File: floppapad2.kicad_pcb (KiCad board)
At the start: 2 copper layers, 76.2 x 76.2 mm, 43 parts, among them J1 USBC, J2 DBG, SW1 SW_Push, SW10 SW_Push, SW11 RotaryEncoder_Switch, SW12 BOOT, SW2 SW_Push, SW3 SW_Push, SW4 SW_Push, SW5 SW_Push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

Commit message: slight adjustment
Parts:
- moved C13 7.47 mm to (63.8, 104.7), turned to -90 degrees
- moved C11 0.91 mm to (59.7, 110.4)
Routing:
- net +3.3V: track 69.0 -> 66.4 mm

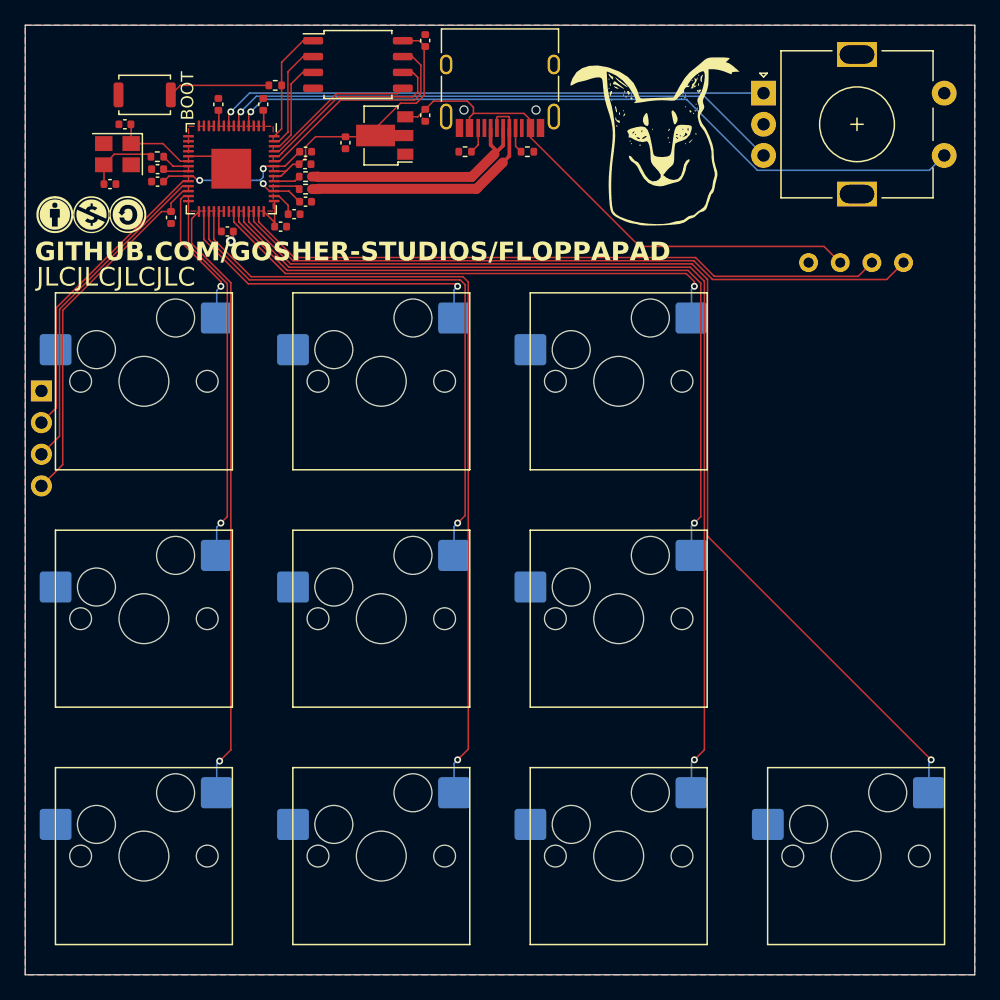
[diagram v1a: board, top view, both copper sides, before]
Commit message: mounting holes
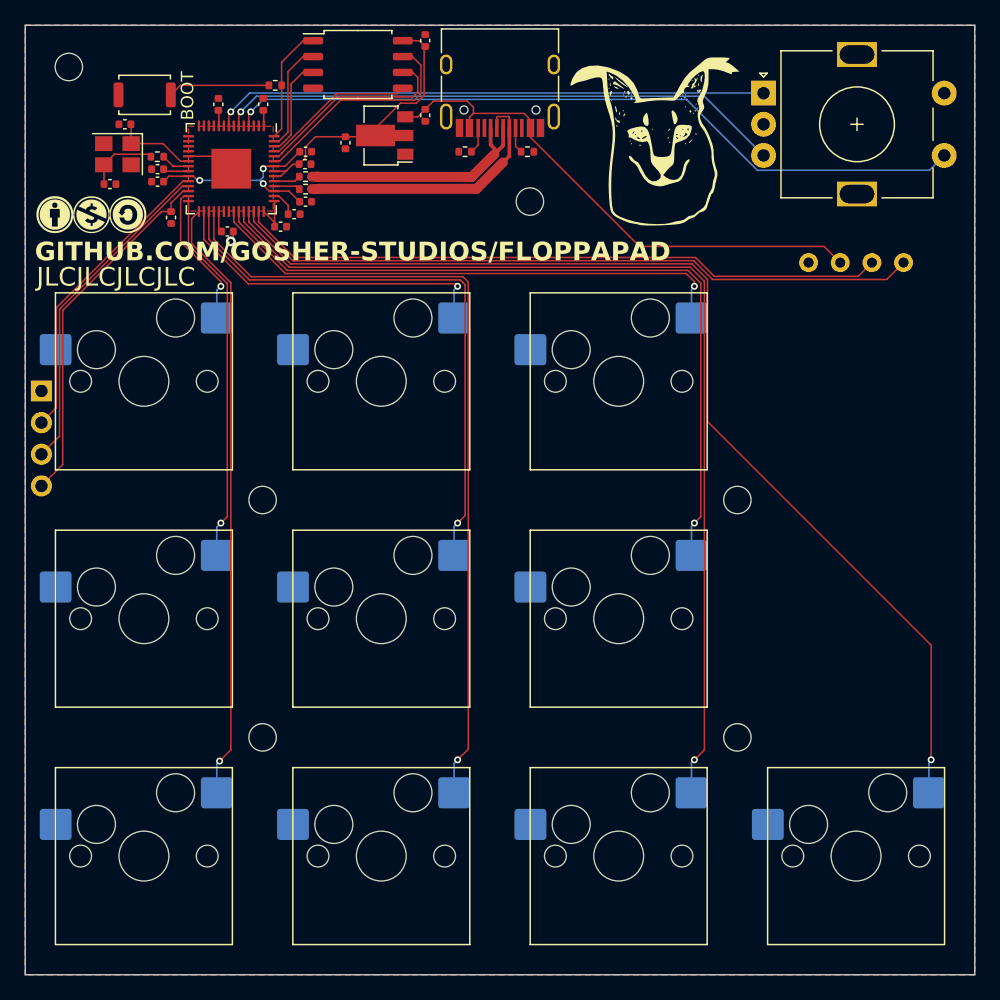
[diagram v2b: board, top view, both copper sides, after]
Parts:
- added REF**: M2, MountingHole:MountingHole_2.2mm_M2, F.Cu at (57.1, 133.3)
- added REF**: M2, MountingHole:MountingHole_2.2mm_M2, F.Cu at (95.2, 133.3)
- added REF**: M2, MountingHole:MountingHole_2.2mm_M2, F.Cu at (78.6, 109.4)
- added REF**: M2, MountingHole:MountingHole_2.2mm_M2, F.Cu at (41.6, 98.6)
- added REF**: M2, MountingHole:MountingHole_2.2mm_M2, F.Cu at (95.2, 152.4)
- added REF**: M2, MountingHole:MountingHole_2.2mm_M2, F.Cu at (57.1, 152.4)
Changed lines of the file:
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@@
     )
   )
+  (footprint "MountingHole:MountingHole_2.2mm_M2" (layer "F.Cu")
+    (at 57.15 133.35)
+    (descr "Mounting Hole 2.2mm, no annular, M2")
+    (tags "mounting hole 2.2mm no annular m2")
+    (attr exclude_from_pos_files exclude_from_bom)
+    (fp_text reference "REF**" (at 0 -3.2) (layer "F.SilkS") hide
+        (effects (font (size 1 1) (thickness 0.15)))
+    )
+    (fp_text value "M2" (at 0 3.2) (layer "F.Fab")
+        (effects (font (size 1 1) (thickness 0.15)))
+    )
+    (fp_text user "${REFERENCE}" (at 0 0) (layer "F.Fab")
+        (effects (font (size 1 1) (thickness 0.15)))
+    )
+    (fp_circle (center 0 0) (end 2.2 0)
+      (stroke (width 0.15) (type solid)) (fill none) (layer "Cmts.User"))
+    (fp_circle (center 0 0) (end 2.45 0)
+      (stroke (width 0.05) (type solid)) (fill none) (layer "F.CrtYd"))
+    (pad "" np_thru_hole circle (at 0 0) (size 2.2 2.2) (drill 2.2) (layers "F&B.Cu" "*.Mask"))
+  )
   (footprint "Package_SO:SOIC-8_5.23x5.23mm_P1.27mm" (layer "F.Cu")
     (at 64.8 98.4)
@@
     )
   )
+  (footprint "MountingHole:MountingHole_2.2mm_M2" (layer "F.Cu")
+    (at 95.25 133.35)
+    (descr "Mounting Hole 2.2mm, no annular, M2")
+    (tags "mounting hole 2.2mm no annular m2")
+    (attr exclude_from_pos_files exclude_from_bom)
+    (fp_text reference "REF**" (at 0 -3.2) (layer "F.SilkS") hide
+        (effects (font (size 1 1) (thickness 0.15)))
+    )
+    (fp_text value "M2" (at 0 3.2) (layer "F.Fab")
+        (effects (font (size 1 1) (thickness 0.15)))
+    )
+    (fp_text user "${REFERENCE}" (at 0 0) (layer "F.Fab")
+        (effects (font (size 1 1) (thickness 0.15)))
+    )
+    (fp_circle (center 0 0) (end 2.2 0)
+      (stroke (width 0.15) (type solid)) (fill none) (layer "Cmts.User"))
+    (fp_circle (center 0 0) (end 2.45 0)
+      (stroke (width 0.05) (type solid)) (fill none) (layer "F.CrtYd"))
+    (pad "" np_thru_hole circle (at 0 0) (size 2.2 2.2) (drill 2.2) (layers "F&B.Cu" "*.Mask"))
+  )
   (footprint "kiswitch:SW_Hotswap_Kailh_MX_1.00u" (layer "F.Cu")
     (at 66.675 123.825)
@@
     )
   )
+  (footprint "MountingHole:MountingHole_2.2mm_M2" (layer "F.Cu")
+    (at 78.6 109.4)
+    (descr "Mounting Hole 2.2mm, no annular, M2")
+    (tags "mounting hole 2.2mm no annular m2")
+    (attr exclude_from_pos_files exclude_from_bom)
+    (fp_text reference "REF**" (at 0 -3.2) (layer "F.SilkS") hide
+        (effects (font (size 1 1) (thickness 0.15)))
+    )
+    (fp_text value "M2" (at 0 3.2) (layer "F.Fab")
+        (effects (font (size 1 1) (thickness 0.15)))
+    )
+    (fp_text user "${REFERENCE}" (at 0 0) (layer "F.Fab")
+        (effects (font (size 1 1) (thickness 0.15)))
+    )
+    (fp_circle (center 0 0) (end 2.2 0)
+      (stroke (width 0.15) (type solid)) (fill none) (layer "Cmts.User"))
+    (fp_circle (center 0 0) (end 2.45 0)
+      (stroke (width 0.05) (type solid)) (fill none) (layer "F.CrtYd"))
+    (pad "" np_thru_hole circle (at 0 0) (size 2.2 2.2) (drill 2.2) (layers "F&B.Cu" "*.Mask"))
+  )
   (footprint "Capacitor_SMD:C_0402_1005Metric" (layer "F.Cu")
     (at 60.595 109.4125)
@@
     )
   )
+  (footprint "MountingHole:MountingHole_2.2mm_M2" (layer "F.Cu")
+    (at 41.6 98.6)
+    (descr "Mounting Hole 2.2mm, no annular, M2")
+    (tags "mounting hole 2.2mm no annular m2")
+    (attr exclude_from_pos_files exclude_from_bom)
+    (fp_text reference "REF**" (at 0 -3.2) (layer "F.SilkS") hide
+        (effects (font (size 1 1) (thickness 0.15)))
+    )
+    (fp_text value "M2" (at 0 3.2) (layer "F.Fab")
+        (effects (font (size 1 1) (thickness 0.15)))
+    )
+    (fp_text user "${REFERENCE}" (at 0 0) (layer "F.Fab")
+        (effects (font (size 1 1) (thickness 0.15)))
+    )
+    (fp_circle (center 0 0) (end 2.2 0)
+      (stroke (width 0.15) (type solid)) (fill none) (layer "Cmts.User"))
+    (fp_circle (center 0 0) (end 2.45 0)
+      (stroke (width 0.05) (type solid)) (fill none) (layer "F.CrtYd"))
+    (pad "" np_thru_hole circle (at 0 0) (size 2.2 2.2) (drill 2.2) (layers "F&B.Cu" "*.Mask"))
+  )
   (footprint "kiswitch:SW_Hotswap_Kailh_MX_1.00u" (layer "F.Cu")
     (at 66.675 142.875)
@@
     )
   )
+  (footprint "MountingHole:MountingHole_2.2mm_M2" (layer "F.Cu")
+    (at 95.25 152.4)
+    (descr "Mounting Hole 2.2mm, no annular, M2")
+    (tags "mounting hole 2.2mm no annular m2")
+    (attr exclude_from_pos_files exclude_from_bom)
+    (fp_text reference "REF**" (at 0 -3.2) (layer "F.SilkS") hide
+        (effects (font (size 1 1) (thickness 0.15)))
+    )
+    (fp_text value "M2" (at 0 3.2) (layer "F.Fab")
+        (effects (font (size 1 1) (thickness 0.15)))
+    )
+    (fp_text user "${REFERENCE}" (at 0 0) (layer "F.Fab")
+        (effects (font (size 1 1) (thickness 0.15)))
+    )
+    (fp_circle (center 0 0) (end 2.2 0)
+      (stroke (width 0.15) (type solid)) (fill none) (layer "Cmts.User"))
+    (fp_circle (center 0 0) (end 2.45 0)
+      (stroke (width 0.05) (type solid)) (fill none) (layer "F.CrtYd"))
+    (pad "" np_thru_hole circle (at 0 0) (size 2.2 2.2) (drill 2.2) (layers "F&B.Cu" "*.Mask"))
+  )
   (footprint "kiswitch:SW_Hotswap_Kailh_MX_1.00u" (layer "F.Cu")
     (at 104.775 161.925)
@@
     )
   )
+  (footprint "MountingHole:MountingHole_2.2mm_M2" (layer "F.Cu")
+    (at 57.15 152.4)
+    (descr "Mounting Hole 2.2mm, no annular, M2")
+    (tags "mounting hole 2.2mm no annular m2")
+    (attr exclude_from_pos_files exclude_from_bom)
+    (fp_text reference "REF**" (at 0 -3.2) (layer "F.SilkS") hide
+        (effects (font (size 1 1) (thickness 0.15)))
+    )
+    (fp_text value "M2" (at 0 3.2) (layer "F.Fab")
+        (effects (font (size 1 1) (thickness 0.15)))
+    )
+    (fp_text user "${REFERENCE}" (at 0 0) (layer "F.Fab")
+        (effects (font (size 1 1) (thickness 0.15)))
+    )
+    (fp_circle (center 0 0) (end 2.2 0)
+      (stroke (width 0.15) (type solid)) (fill none) (layer "Cmts.User"))
+    (fp_circle (center 0 0) (end 2.45 0)
+      (stroke (width 0.05) (type solid)) (fill none) (layer "F.CrtYd"))
+    (pad "" np_thru_hole circle (at 0 0) (size 2.2 2.2) (drill 2.2) (layers "*.Cu" "*.Mask"))
+  )
   (footprint "floppapad2:floppa" (layer "F.Cu")
     (at 88.6 104.6)
@@
   (segment (start 72.517 135.483) (end 72.8 135.2) (width 0.127) (layer "B.Cu") (net 25))
   (segment (start 72.517 137.795) (end 72.517 135.483) (width 0.127) (layer "B.Cu") (net 25))
-  (segment (start 55.2375 110.2) (end 55.2375 111.0375) (width 0.127) (layer "F.Cu") (net 26))
-  (segment (start 92.3135 115.950401) (end 92.3135 134.6865) (width 0.127) (layer "F.Cu") (net 26))
-  (segment (start 92.3135 134.6865) (end 91.8 135.2) (width 0.127) (layer "F.Cu") (net 26))
   (segment (start 59.1245 114.9245) (end 91.287599 114.9245) (width 0.127) (layer "F.Cu") (net 26))
+  (segment (start 92.3135 134.6865) (end 91.8 135.2) (width 0.127) (layer "F.Cu") (net 26))
   (segment (start 55.2375 111.0375) (end 59.1245 114.9245) (width 0.127) (layer "F.Cu") (net 26))
+  (segment (start 55.2375 110.2) (end 55.2375 111.0375) (width 0.127) (layer "F.Cu") (net 26))
+  (segment (start 92.3135 115.950401) (end 92.3135 134.6865) (width 0.127) (layer "F.Cu") (net 26))
   (segment (start 91.287599 114.9245) (end 92.3135 115.950401) (width 0.127) (layer "F.Cu") (net 26))
   (via (at 91.8 135.2) (size 0.56) (drill 0.3) (layers "F.Cu" "B.Cu") (net 26))
@@
   (segment (start 91.8 154.2) (end 91.567 154.433) (width 0.127) (layer "B.Cu") (net 29))
   (segment (start 91.567 154.433) (end 91.567 156.845) (width 0.127) (layer "B.Cu") (net 29))
-  (segment (start 56.0375 110.2) (end 56.0375 111.0375) (width 0.127) (layer "F.Cu") (net 30))
   (segment (start 56.0375 111.0375) (end 59.4 114.4) (width 0.127) (layer "F.Cu") (net 30))
-  (segment (start 92.854 136.254) (end 110.8 154.2) (width 0.127) (layer "F.Cu") (net 30))
-  (segment (start 59.4 114.4) (end 91.6 114.4) (width 0.127) (layer "F.Cu") (net 30))
-  (segment (start 92.854 115.654) (end 92.854 136.254) (width 0.127) (layer "F.Cu") (net 30))
+  (segment (start 110.8 145) (end 110.8 154.2) (width 0.127) (layer "F.Cu") (net 30))
+  (segment (start 92.854 127.054) (end 110.8 145) (width 0.127) (layer "F.Cu") (net 30))
+  (segment (start 56.0375 110.2) (end 56.0375 111.0375) (width 0.127) (layer "F.Cu") (net 30))
+  (segment (start 92.854 115.654) (end 92.854 127.054) (width 0.127) (layer "F.Cu") (net 30))
   (segment (start 91.6 114.4) (end 92.854 115.654) (width 0.127) (layer "F.Cu") (net 30))
+  (segment (start 59.4 114.4) (end 91.6 114.4) (width 0.127) (layer "F.Cu") (net 30))
   (via (at 110.8 154.2) (size 0.56) (drill 0.3) (layers "F.Cu" "B.Cu") (net 30))
   (segment (start 110.617 154.383) (end 110.8 154.2) (width 0.127) (layer "B.Cu") (net 30))

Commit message: better debug
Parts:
- removed J2: DBG, Connector_PinSocket_2.54mm:PinSocket_1x04_P2.54mm_Vertical
- added DBG: DBG, Connector_PinSocket_2.54mm:PinSocket_1x03_P2.54mm_Vertical, F.Cu at (39.8, 115.4)
- moved C5 0.60 mm to (49.8, 110.1)
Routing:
- net +3.3V: track 66.4 -> 39.1 mm
- net SWD: track 26.7 -> 10.4 mm
- net SWCLK: track 24.5 -> 12.0 mm
- net GND: track 5.26 -> 7.28 mm
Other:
- board text added: "github.com/gosher-studios/floppapad"
- board text removed: "GITHUB.COM/GOSHER-STUDIOS/FLOPPAPAD"
